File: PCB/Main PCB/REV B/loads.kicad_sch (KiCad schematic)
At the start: 17 parts, among them J10 Auger, J11 Ignitor, J9 FAN, U12 TLP2362TPR_E, U7 ALDP105W, U8 TLP2362TPR_E, U9 TLP2362TPR_E

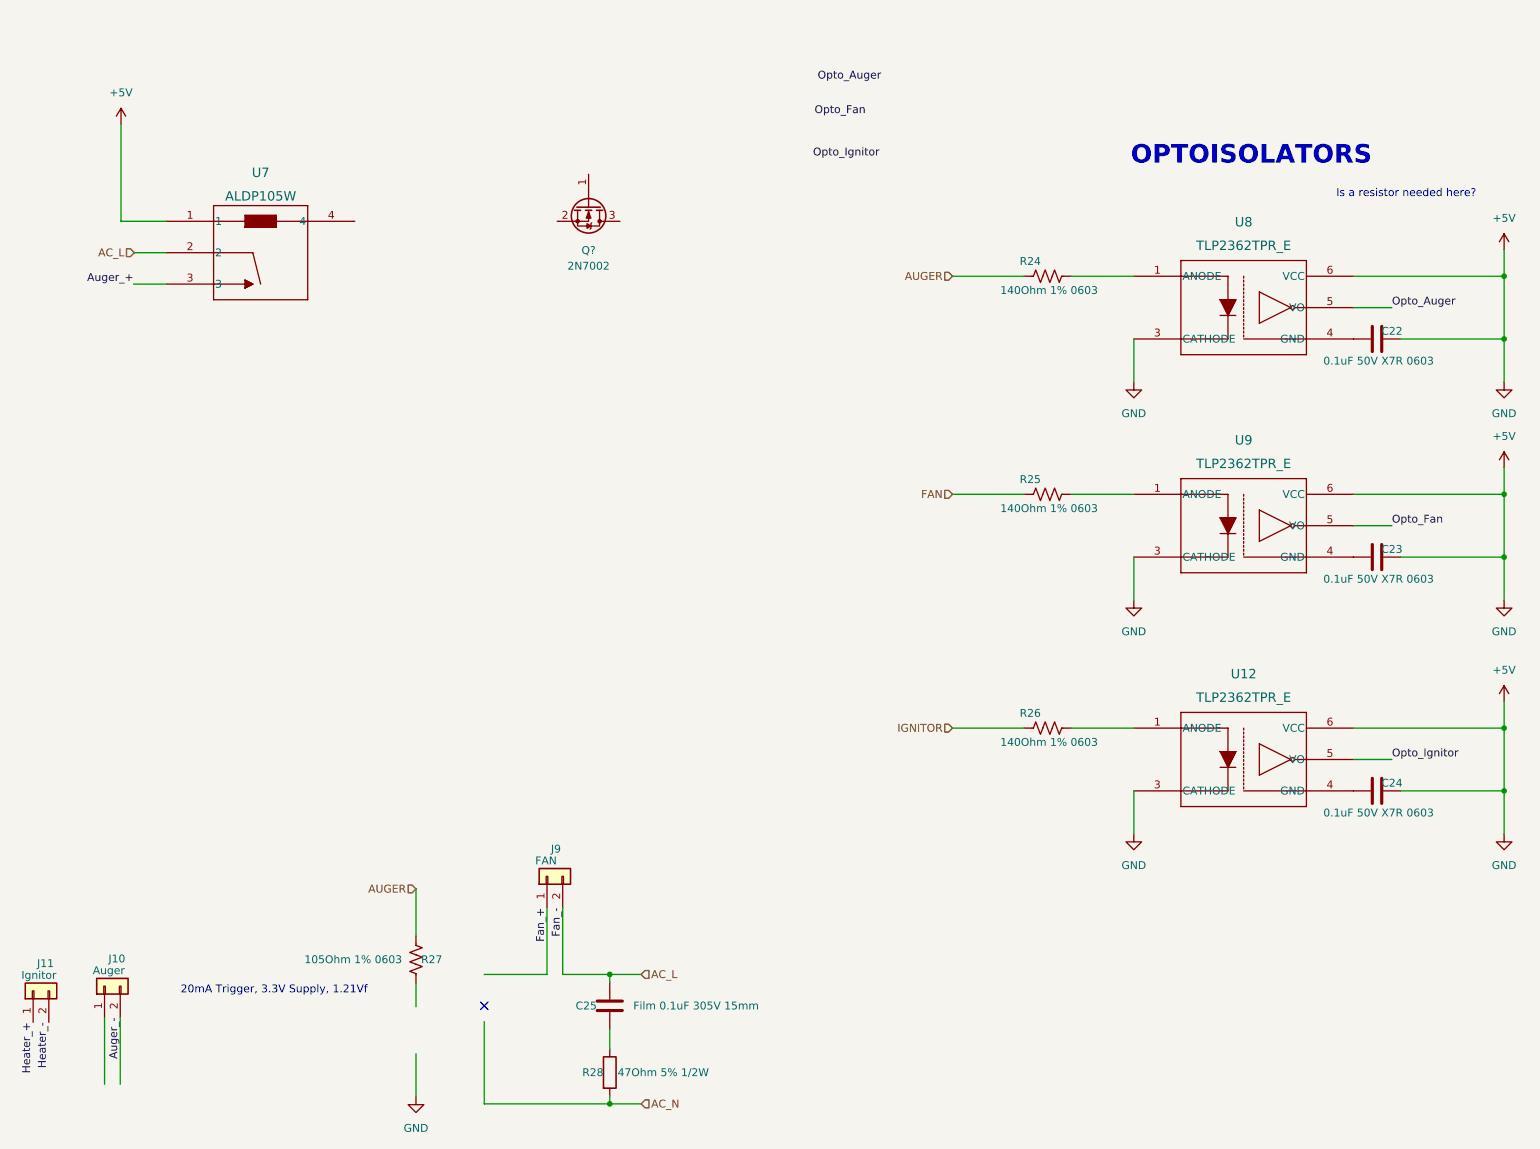
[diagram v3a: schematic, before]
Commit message: PCB schematic updates, Relay Circuits Completed
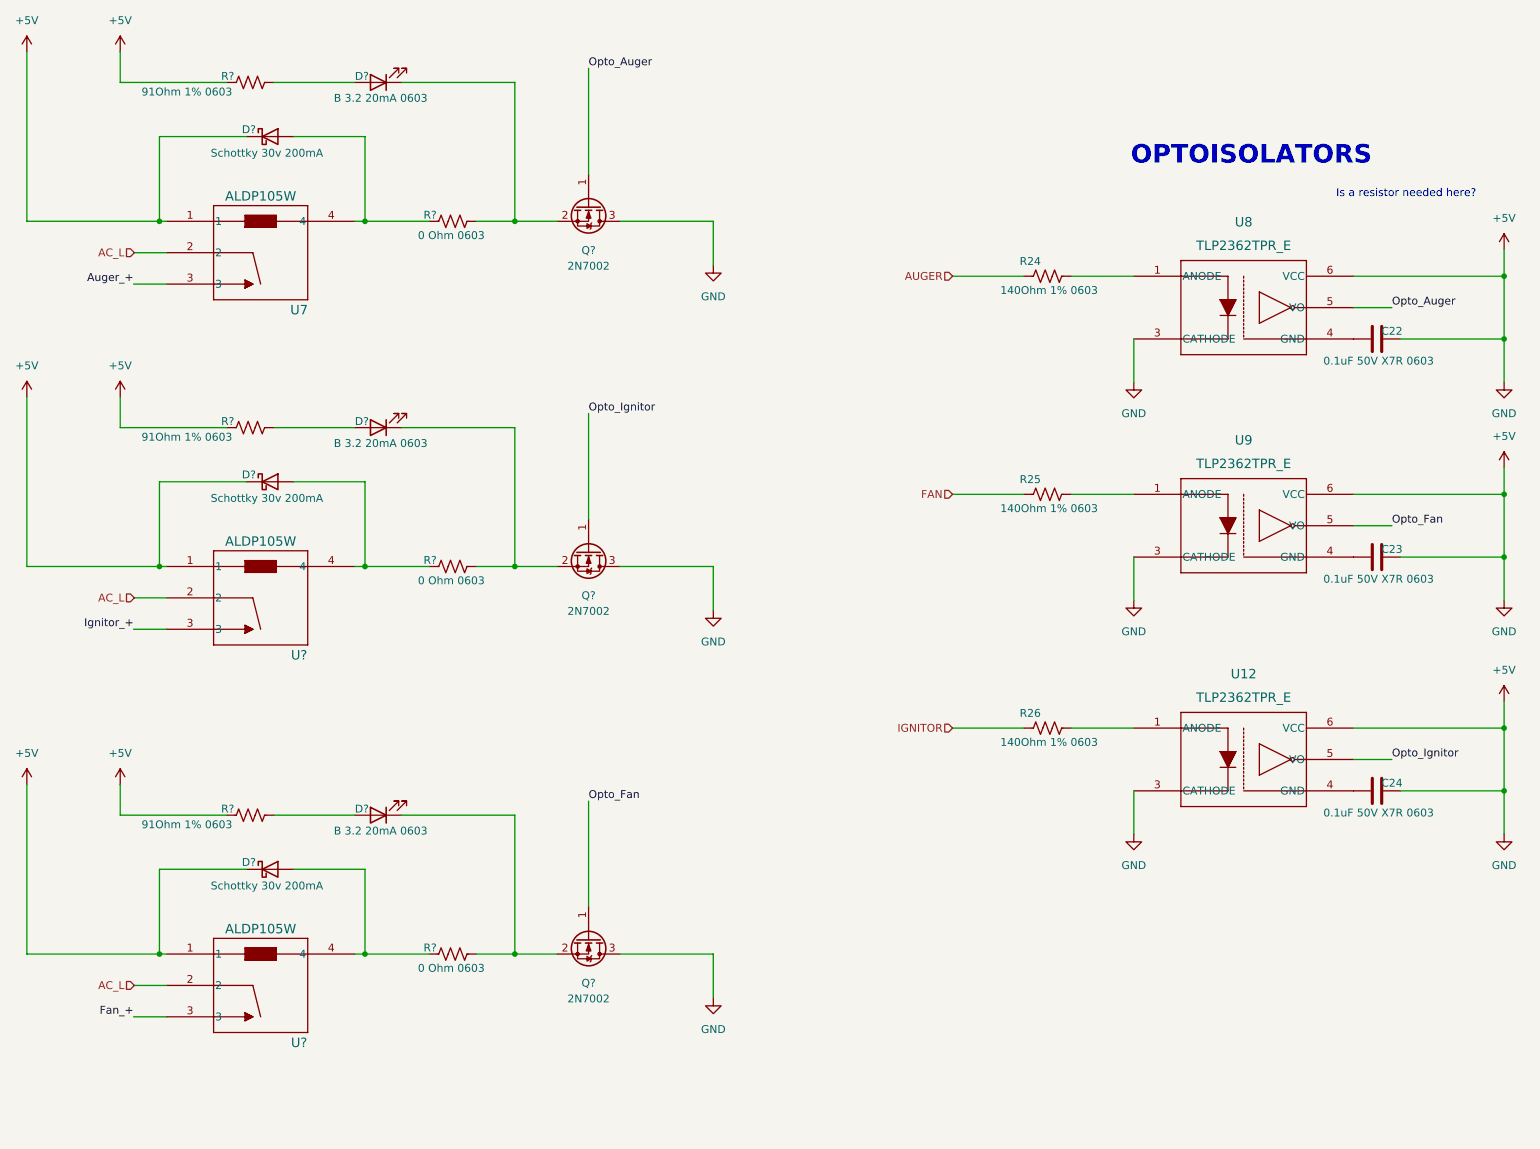
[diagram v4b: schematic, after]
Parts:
- removed C25: Film 0.1uF 305V 15mm, Capacitor_THT:C_Rect_L18.0mm_W6.0mm_P15.00mm_FKS3_FKP3, symbol Device:C
- removed J10: Auger, TestPoint:TestPoint_2Pads_Pitch5.08mm_Drill1.3mm, symbol Connector_Generic:Conn_01x02
- removed J11: Ignitor, TestPoint:TestPoint_2Pads_Pitch5.08mm_Drill1.3mm, symbol Connector_Generic:Conn_01x02
- removed J9: FAN, TestPoint:TestPoint_2Pads_Pitch5.08mm_Drill1.3mm, symbol Connector_Generic:Conn_01x02
- removed R27: 105Ohm 1% 0603, Resistor_SMD:R_0603_1608Metric, symbol Device:R_US
- removed R28: 47Ohm 5% 1/2W, Resistor_THT:R_Axial_DIN0204_L3.6mm_D1.6mm_P5.08mm_Vertical, symbol Device:R
- added D? (x3): Schottky 30v 200mA, Customs Smoker:RB521S30T1G-M, symbol Diode:1N6857UR
- added D? (x3): B 3.2 20mA 0603, LED_SMD:LED_0603_1608Metric, symbol Device:LED
- added Q? (x2): 2N7002, Package_TO_SOT_SMD:SOT-23, symbol Transistor_FET:2N7002
- added R? (x3): 0 Ohm 0603, Resistor_SMD:R_0603_1608Metric, symbol Device:R_US
- added R? (x3): 91Ohm 1% 0603, Resistor_SMD:R_0603_1608Metric, symbol Device:R_US
- added U? (x2): ALDP105W, Customs Smoker:PAN_ALD_PAN, symbol ALDP105W:ALDP105W
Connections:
- net +5V: now also Q?.3 (D), D?.1 (K), D?.1 (K), D?.1 (K), Q?.3 (D), Q?.3 (D), R?.1, R?.1, R?.1, U?.1, U?.1
- net AC_L: now also U?.2, U?.2
- net Fan_+: now also U?.3
- net Opto_Auger: now also Q?.1 (G)
- net Opto_Fan: now also Q?.1 (G)
- net Opto_Ignitor: now also Q?.1 (G)
- net at U7.4: now also D?.2 (A), R?.1
- net at Q?.2 (S): now also D?.1 (K), R?.2
- new net: D?.2 (A), R?.1, U?.4 (x2)
- new net: D?.1 (K), Q?.2 (S), R?.2 (x2)
- new net: D?.2 (A), R?.2 (x3)
- new net Ignitor_+: U?.3
- no-connect marks 1 -> 0
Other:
- note removed: "20mA Trigger, 3.3V Supply, 1.21Vf"

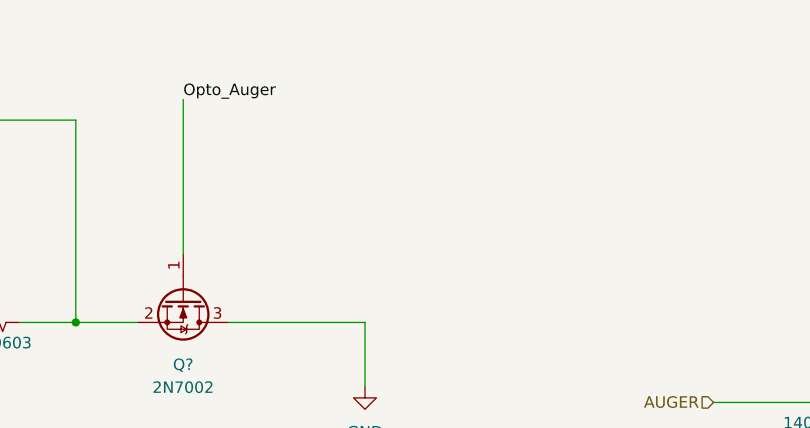
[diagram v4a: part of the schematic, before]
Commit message: PCB schematic updates, Thermocouple connector sourced and updated
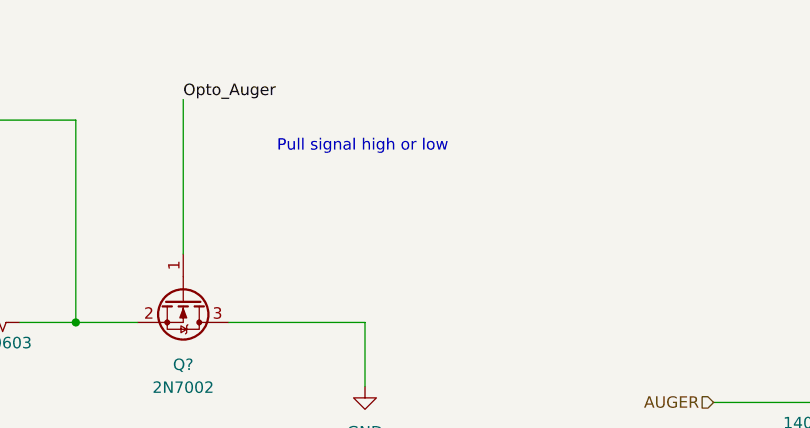
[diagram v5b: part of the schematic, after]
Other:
- note added: "Pull signal high or low"

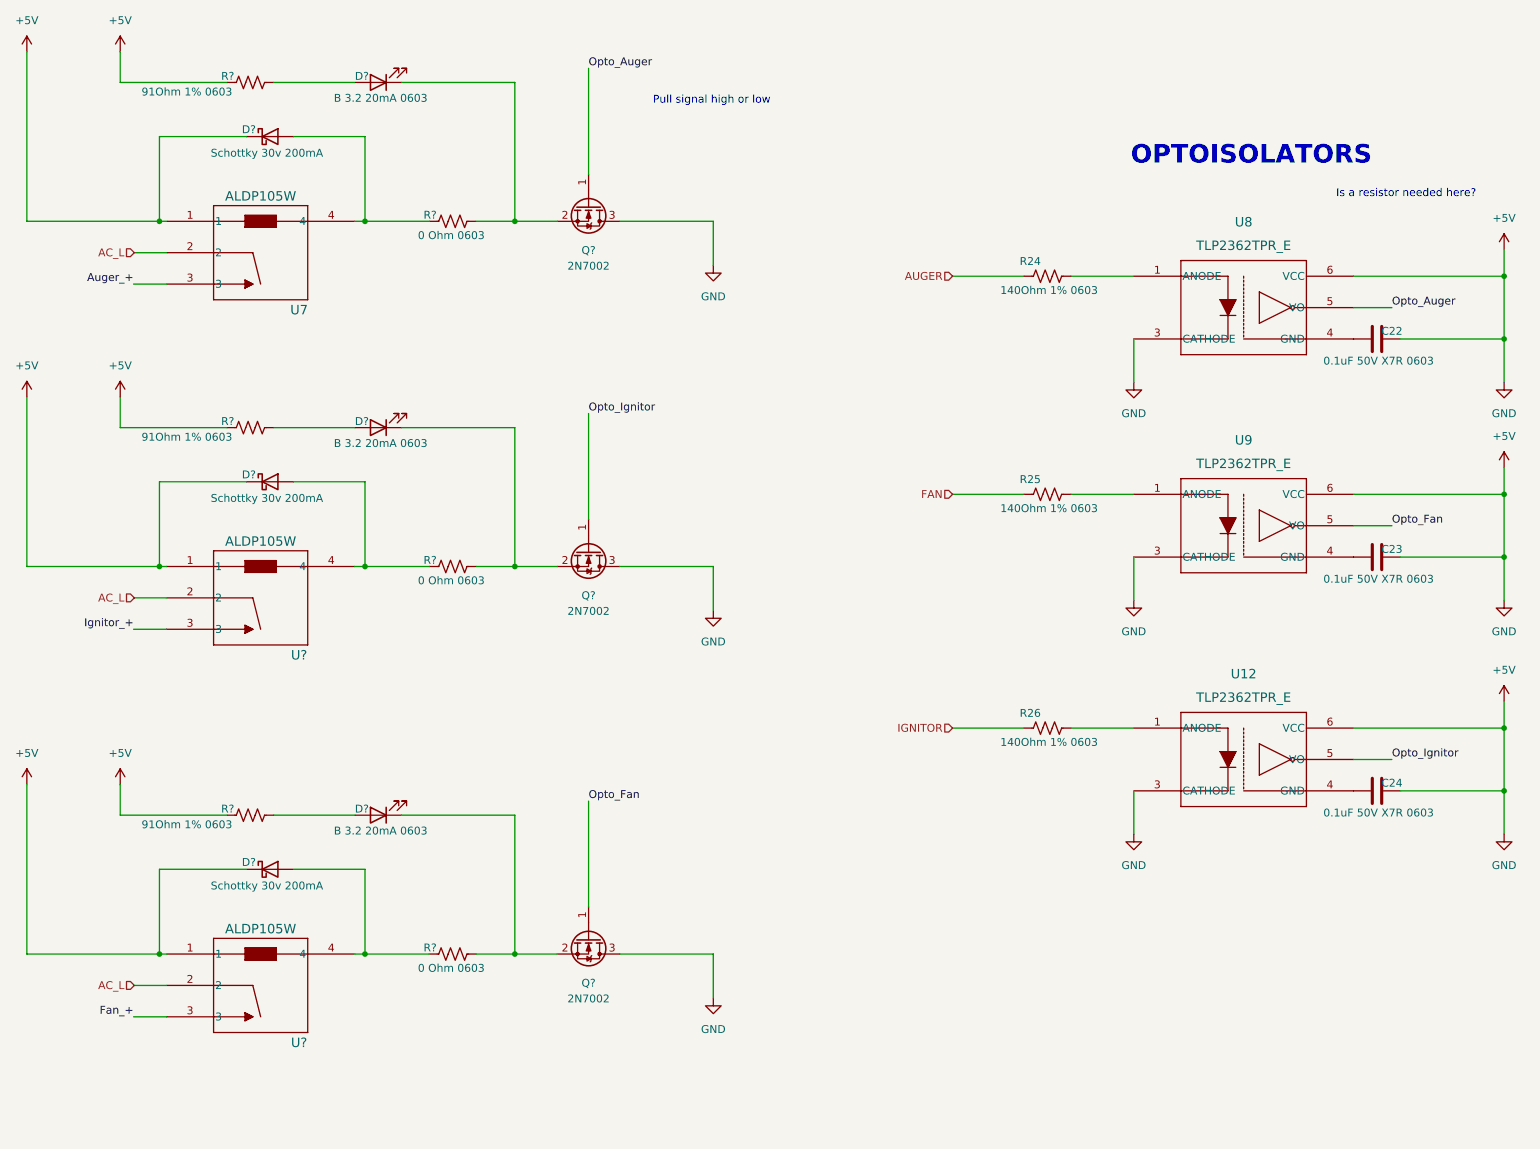
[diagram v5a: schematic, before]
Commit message: PCB schematic updates, Screen and Probe jack updates
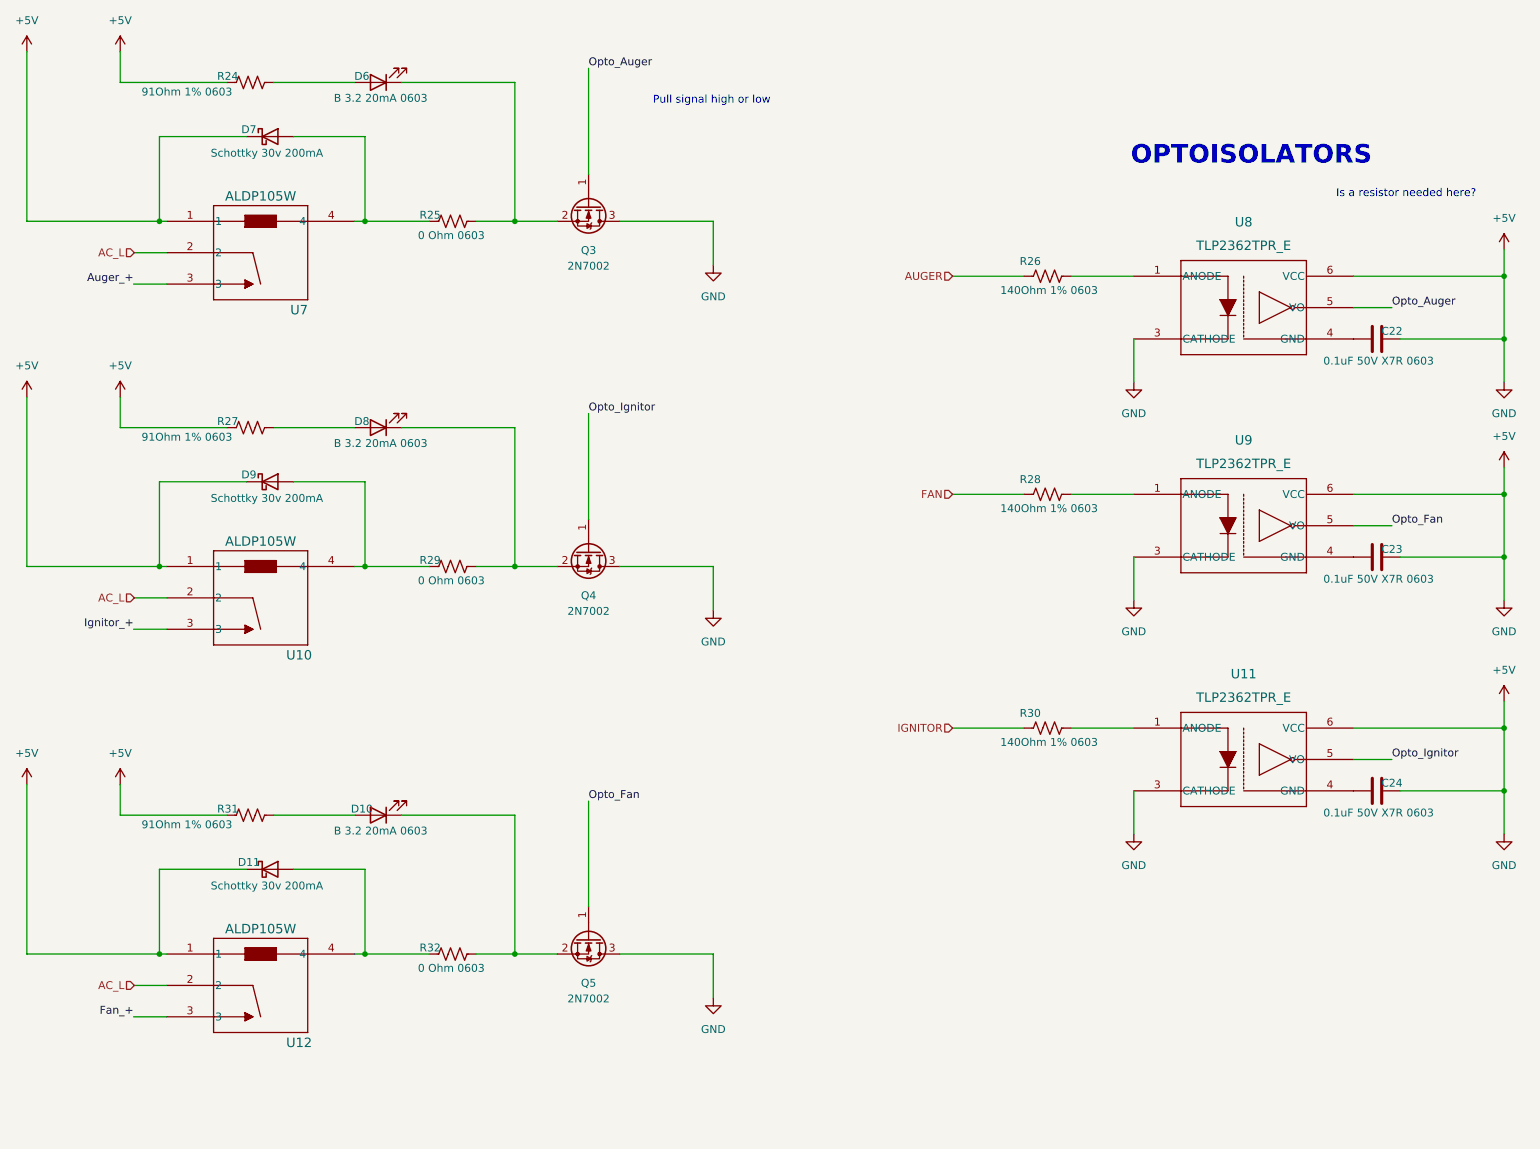
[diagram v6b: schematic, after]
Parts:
- gave numbers to parts that had none: 17
- renumbered R24 to R26, R25 to R28, R26 to R30, U12 to U11

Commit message: PCB schematic updates, Change to smaller thermocouple mux
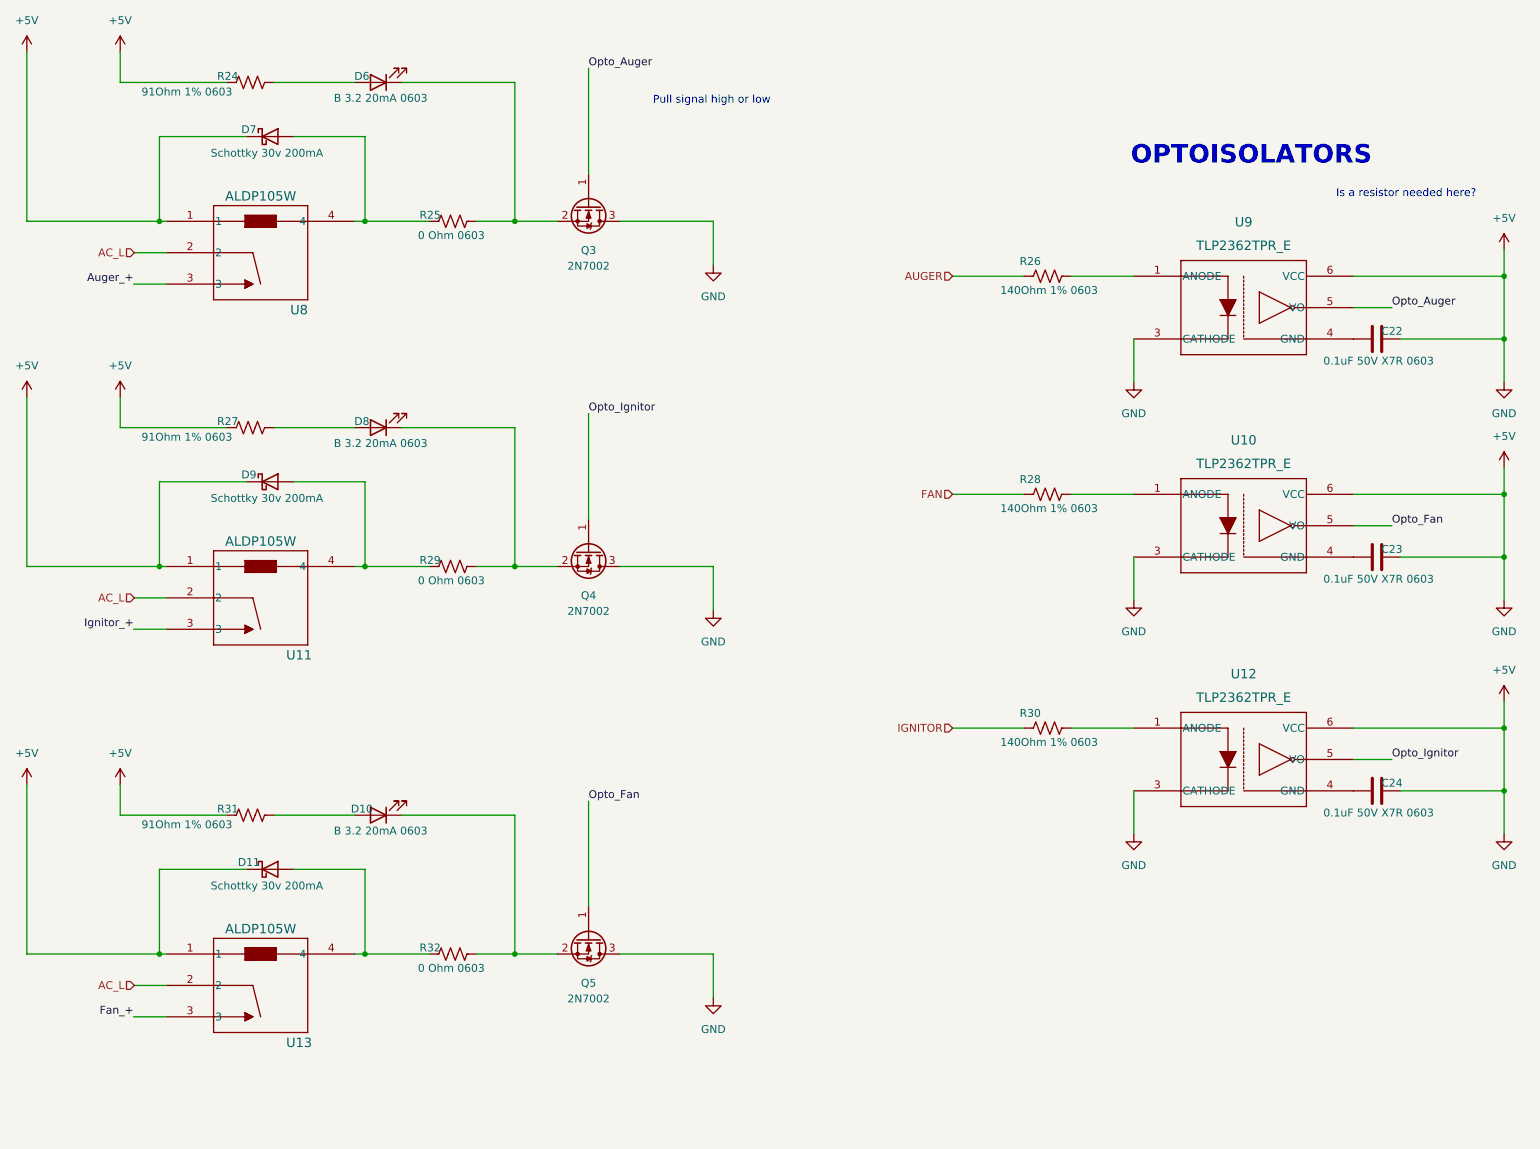
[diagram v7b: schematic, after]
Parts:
- renumbered U9 to U10, U10 to U11, U11 to U12, U12 to U13, U7 to U8, U8 to U9
